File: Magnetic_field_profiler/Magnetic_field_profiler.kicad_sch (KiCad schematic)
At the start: 71 parts, among them J1 USB_B_Micro, J2 Barrel_Jack_Switch, J3 Conn_01x04_Socket, Q1 BSS123, SW1 SW_SPDT, U1 STM32F103C8Tx, U10 MLX90393, U11 MLX90393, U12 MLX90393, U2 AP2112K-3.3, U3 DRV8825, U4 MLX90393, U5 MLX90393, U6 MLX90393, U7 MLX90393, U8 MLX90393, U9 MLX90393, Y1 Crystal_GND24

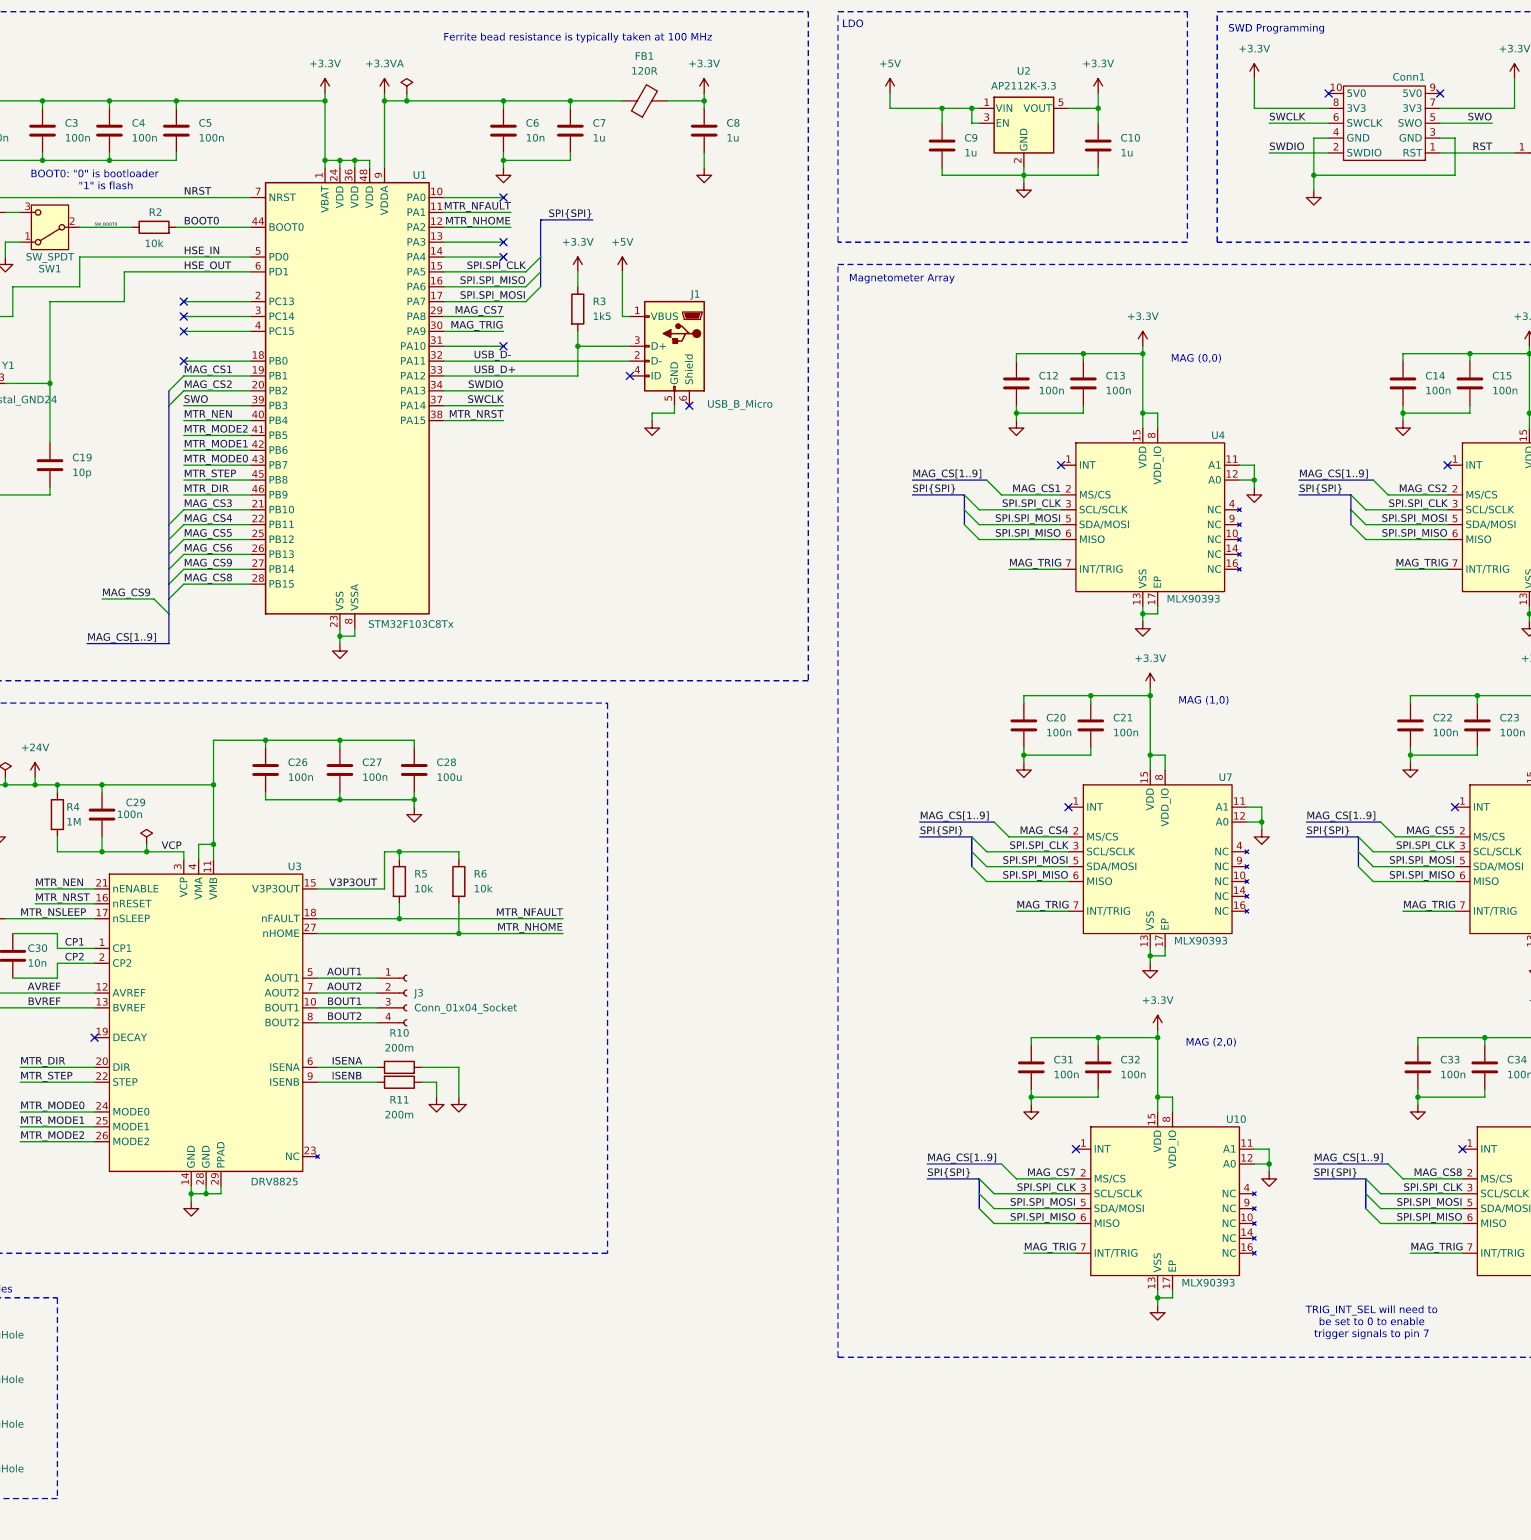
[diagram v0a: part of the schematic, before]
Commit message: SMPS Added, Edge Cuts Modified
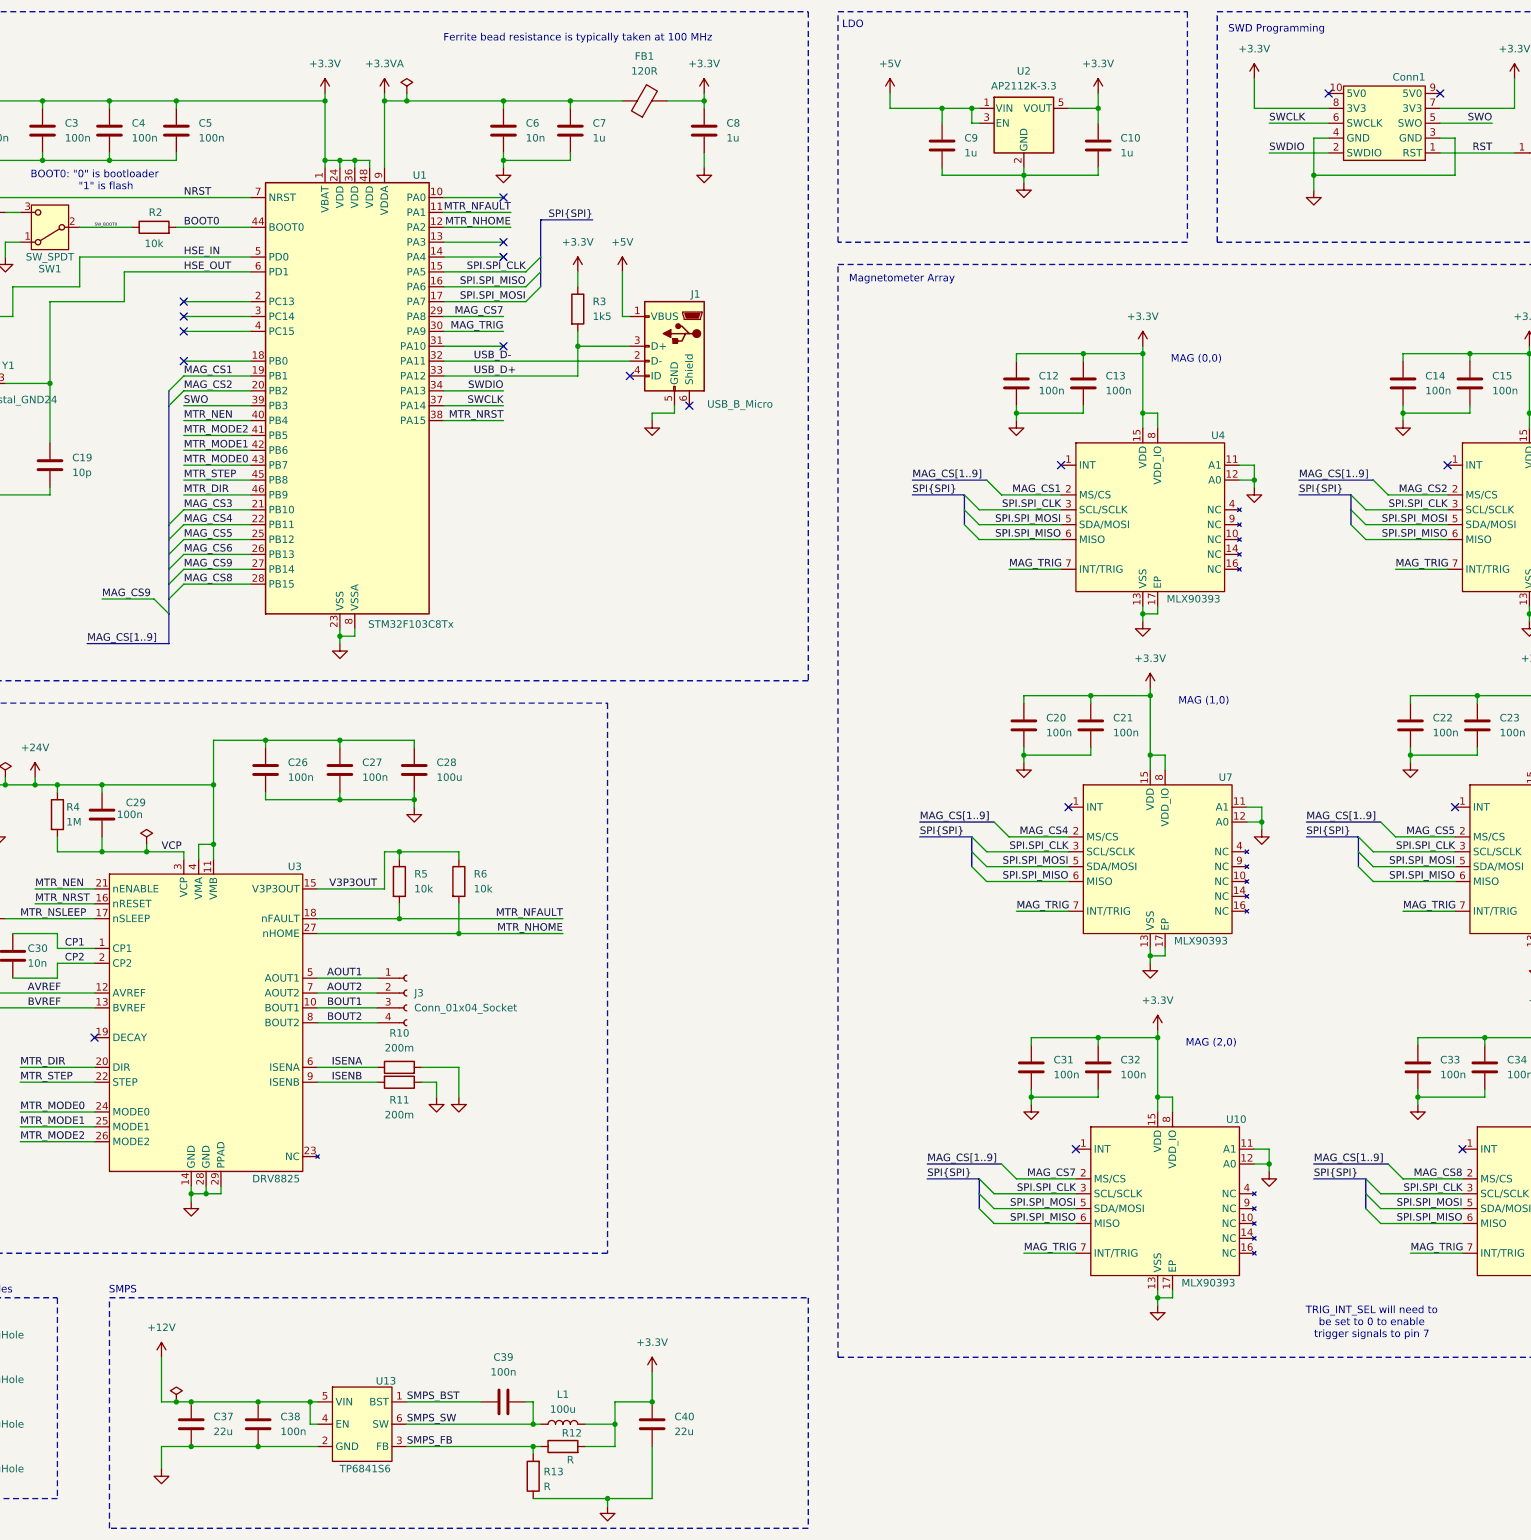
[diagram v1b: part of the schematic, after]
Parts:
- added C37, C40: 22u, Capacitor_SMD:C_0603_1608Metric, symbol Device:C
- added C38, C39: 100n, Capacitor_SMD:C_0402_1005Metric, symbol Device:C
- added L1: 100u, Inductor_SMD:L_0603_1608Metric, symbol Device:L
- added R12, R13: R, Resistor_SMD:R_0402_1005Metric, symbol Device:R
- added U13: TP6841S6, Package_TO_SOT_SMD:SOT-23-6, symbol Mag_Profiler_ICs:TP6841S6
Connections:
- net +3.3V: now also C40.1, L1.2, R12.2
- net GND: now also C37.2, C38.2, C40.2, R13.1, U13.2 (GND)
- new net +12V: C37.1, C38.1, U13.4 (EN), U13.5 (VIN)
- new net SMPS_BST: C39.1, U13.1 (BST)
- new net SMPS_FB: R12.1, R13.2, U13.3 (FB)
- new net SMPS_SW: C39.2, L1.1, U13.6 (SW)
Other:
- note added: "SMPS"

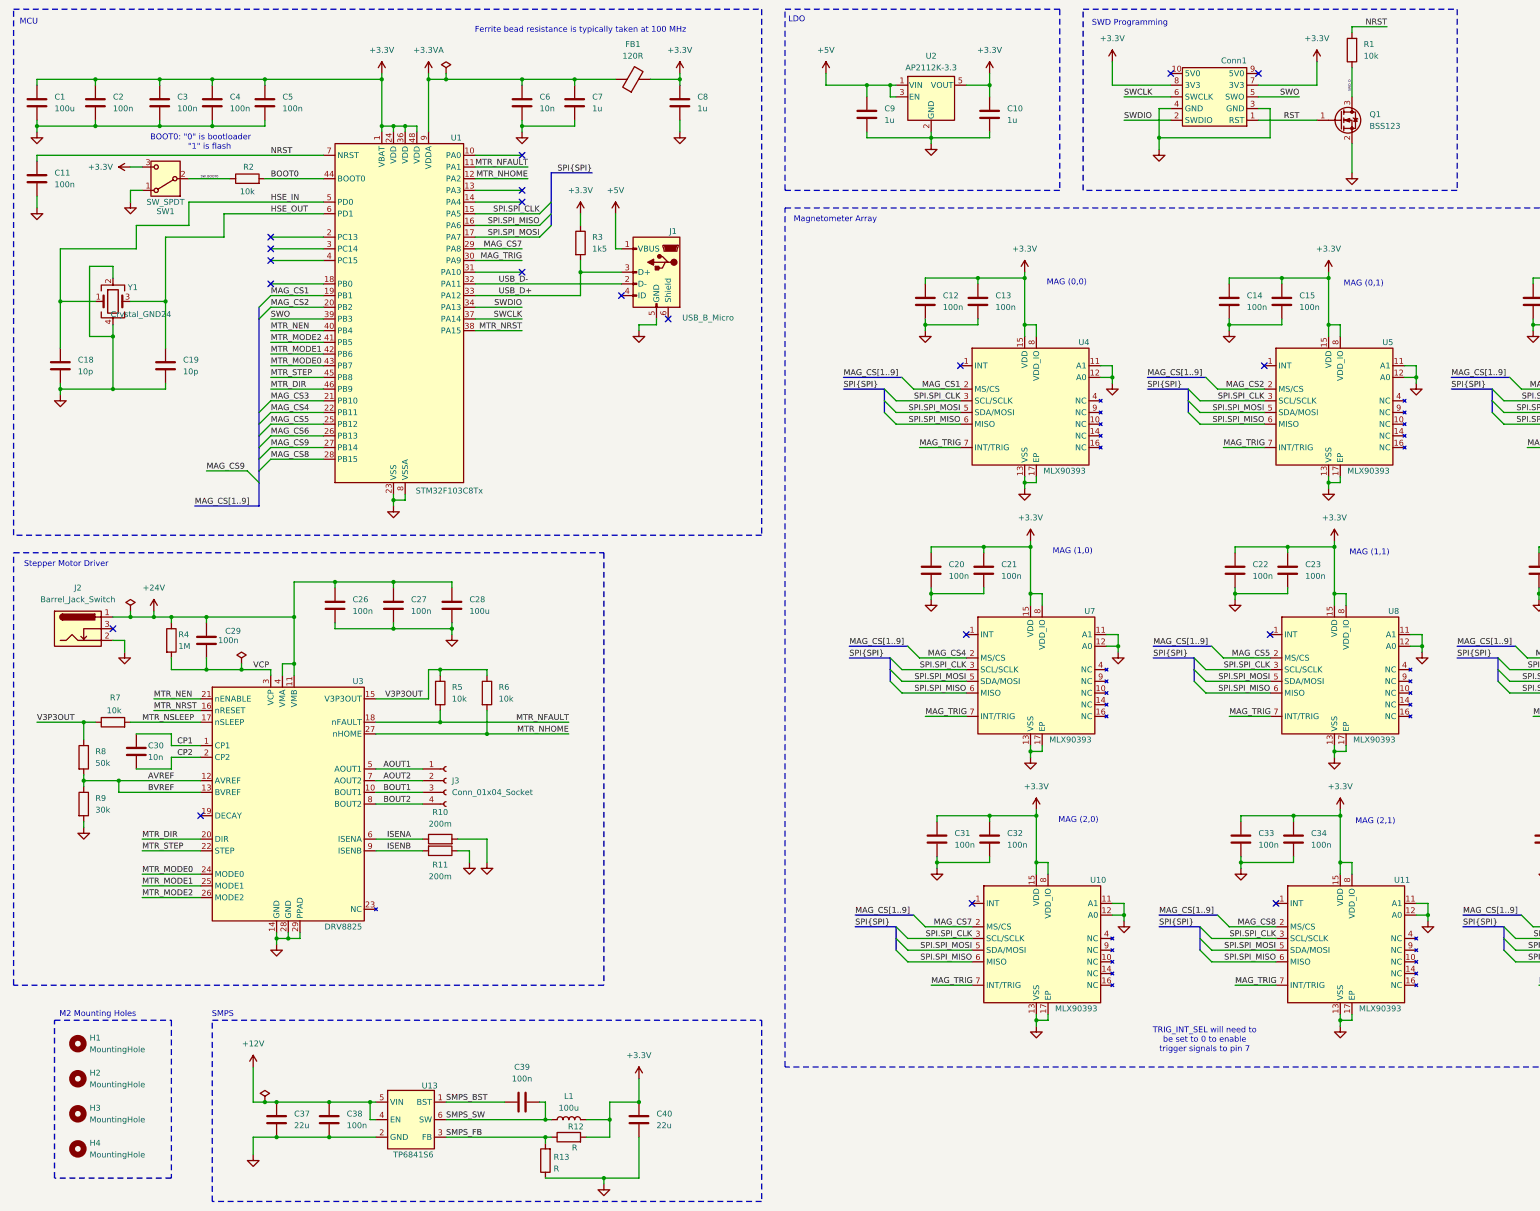
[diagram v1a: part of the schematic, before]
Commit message: Added SMPS and removed LDO
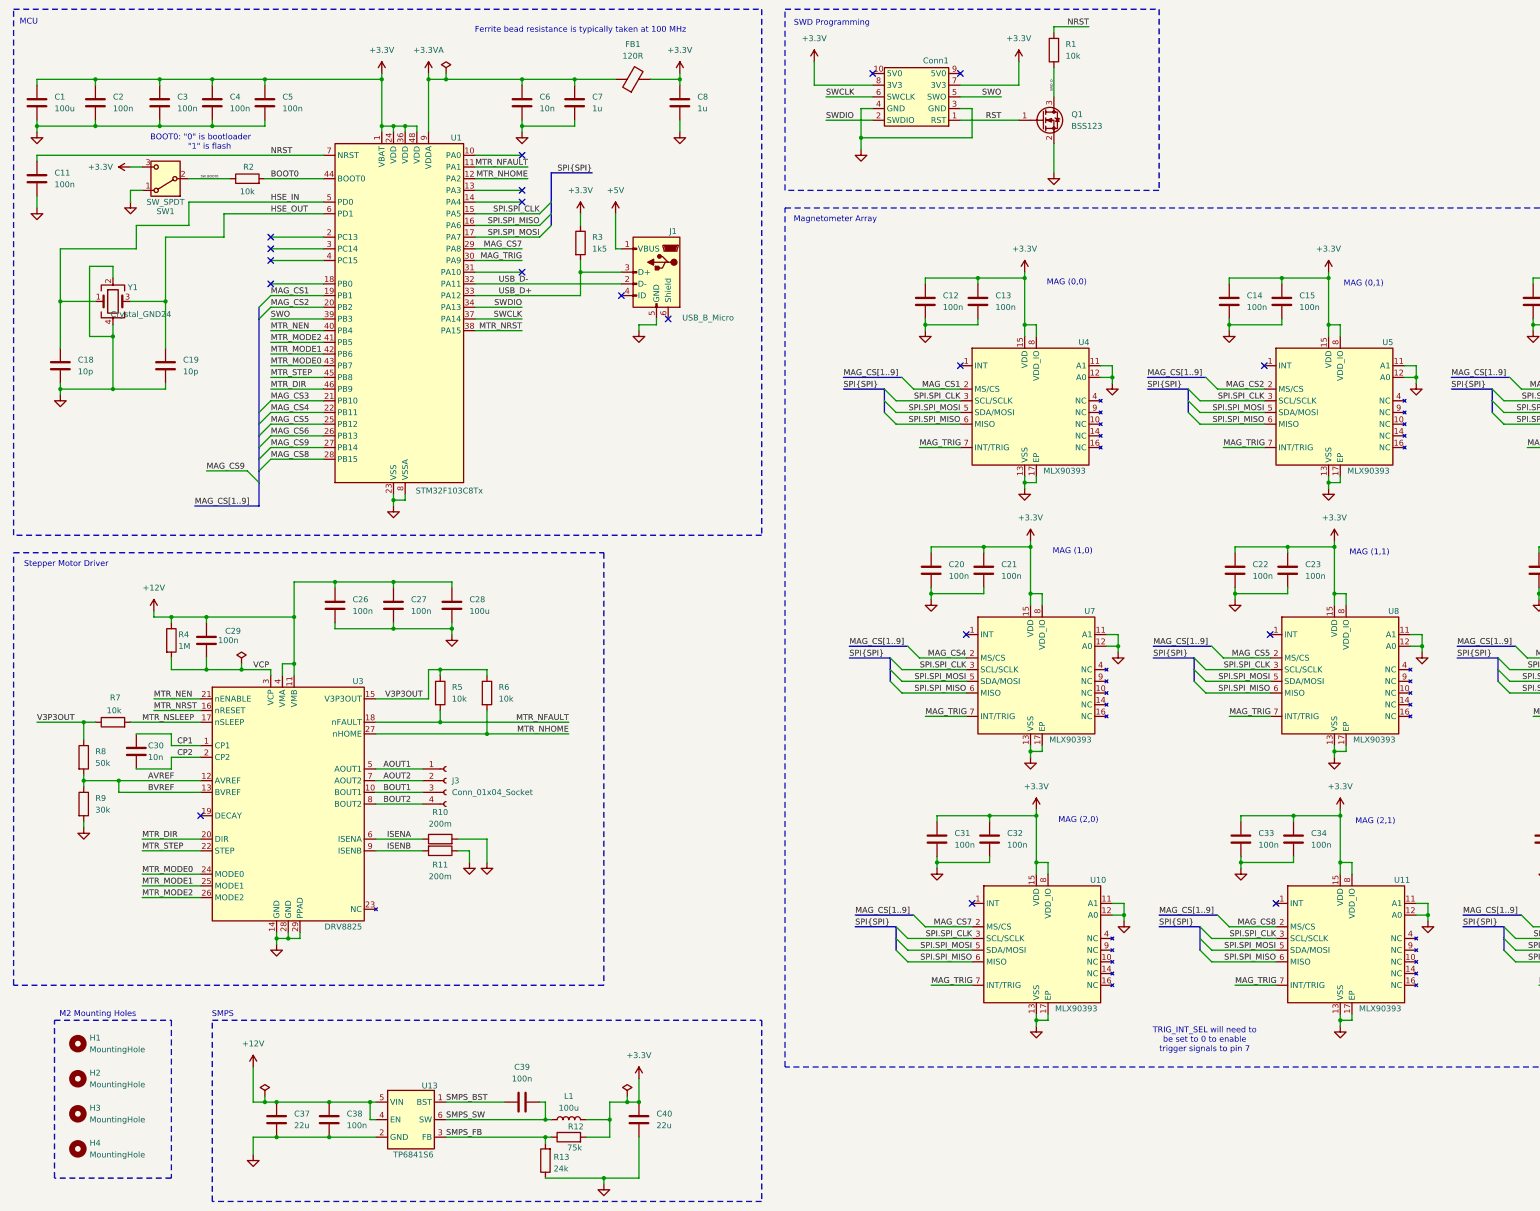
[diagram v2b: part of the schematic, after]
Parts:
- removed C10, C9: 1u, Capacitor_SMD:C_0603_1608Metric, symbol Device:C
- removed J2: Barrel_Jack_Switch, Connector_BarrelJack:BarrelJack_Kycon_KLDX-0202-xC_Horizontal, symbol Connector:Barrel_Jack_Switch
- removed U2: AP2112K-3.3, Package_TO_SOT_SMD:SOT-23-5, symbol Regulator_Linear:AP2112K-3.3
- R12: value R -> 75k
- R13: value R -> 24k
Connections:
- net +24V is gone; now on net +12V: C26.1, C27.1, C28.1, C29.1, R4.1, U3.11 (VMB), U3.4 (VMA)
- no-connect marks 23 -> 22
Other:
- note removed: "LDO"
- moved on the sheet: Conn1, Q1, R1

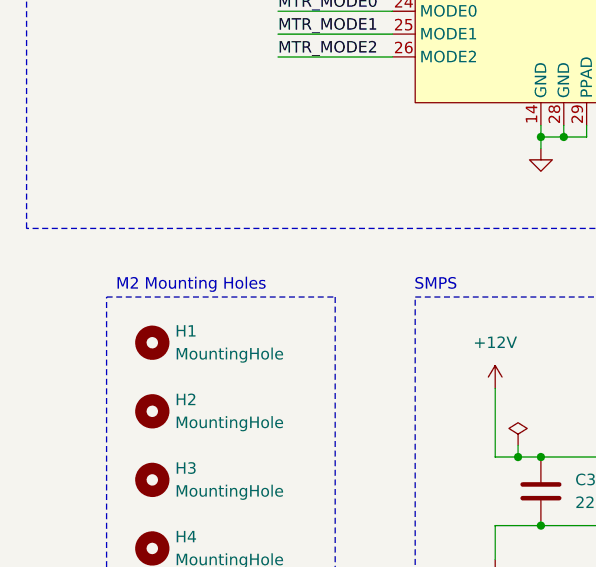
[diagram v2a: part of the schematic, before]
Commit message: Edge cuts updated
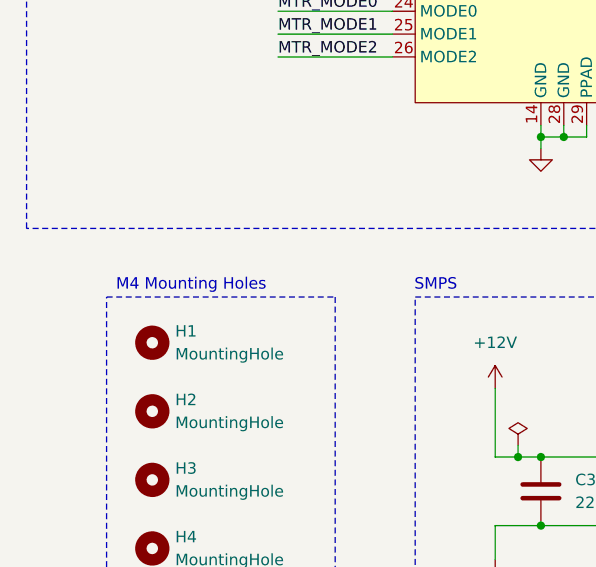
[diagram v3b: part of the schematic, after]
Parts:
- H1, H2, H3, H4: footprint MountingHole:MountingHole_2.2mm_M2 -> MountingHole:MountingHole_3.2mm_M3
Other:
- note added: "M4 Mounting Holes"
- note removed: "M2 Mounting Holes"
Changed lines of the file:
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@@
 		)
 	)
-	(text "M2 Mounting Holes"
+	(text "M4 Mounting Holes"
 		(exclude_from_sim no)
 		(at 36.068 236.22 0)
@@
 			)
 		)
-		(property "Footprint" "MountingHole:MountingHole_2.2mm_M2"
+		(property "Footprint" "MountingHole:MountingHole_3.2mm_M3"
 			(at 31.75 242.57 0)
 			(effects
@@
 			)
 		)
-		(property "Footprint" "MountingHole:MountingHole_2.2mm_M2"
+		(property "Footprint" "MountingHole:MountingHole_3.2mm_M3"
 			(at 31.75 250.19 0)
 			(effects
@@
 			)
 		)
-		(property "Footprint" "MountingHole:MountingHole_2.2mm_M2"
+		(property "Footprint" "MountingHole:MountingHole_3.2mm_M3"
 			(at 31.75 257.81 0)
 			(effects
@@
 			)
 		)
-		(property "Footprint" "MountingHole:MountingHole_2.2mm_M2"
+		(property "Footprint" "MountingHole:MountingHole_3.2mm_M3"
 			(at 31.75 265.43 0)
 			(effects
